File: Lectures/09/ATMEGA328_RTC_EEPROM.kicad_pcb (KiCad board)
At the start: 2 copper layers, 50.8 x 53.3 mm, 44 parts, among them J1 Serial, J2 Digital 1, J3 I2C, J4 ICSP, J5 Digital 2, Q1 IRLML6401, SW1 SW_SPST, U1 ATmega328P-AU, U2 24LC1025, U3 24LC1025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

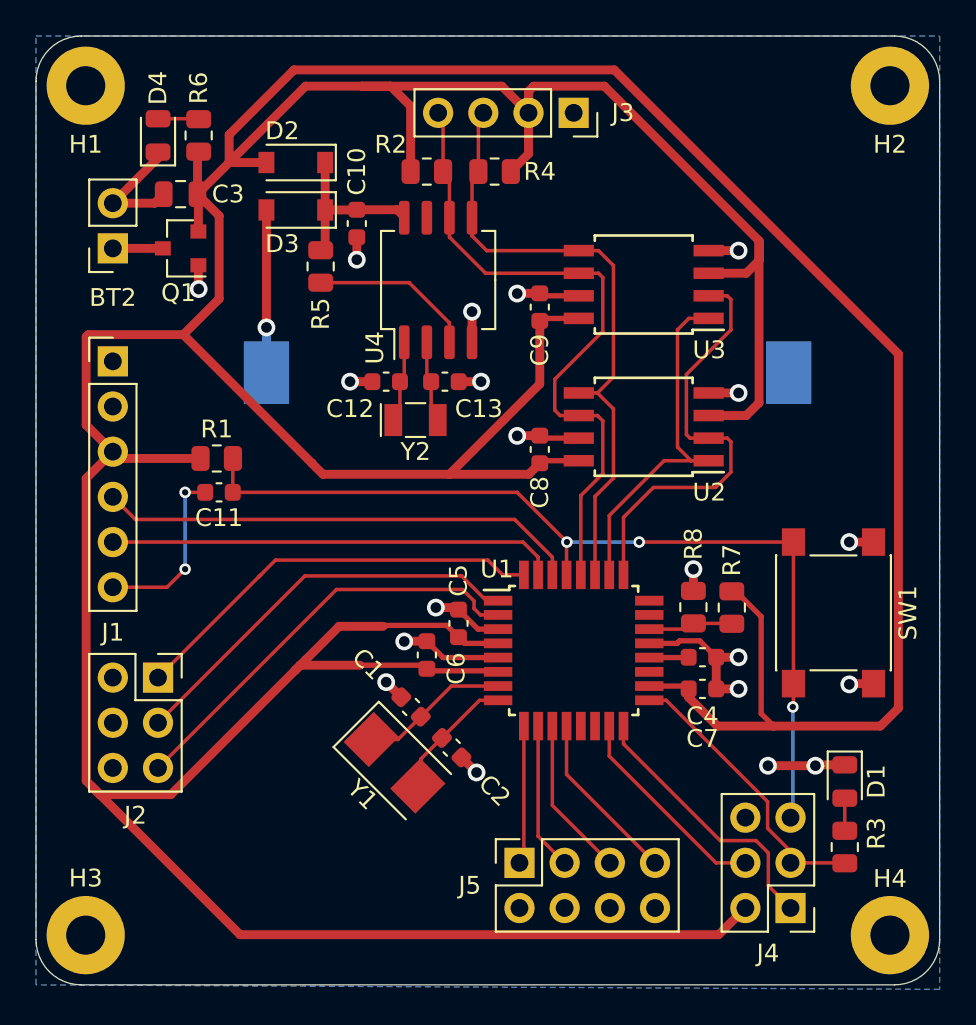
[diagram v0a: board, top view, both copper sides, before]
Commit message: Addressing and Silkscreen
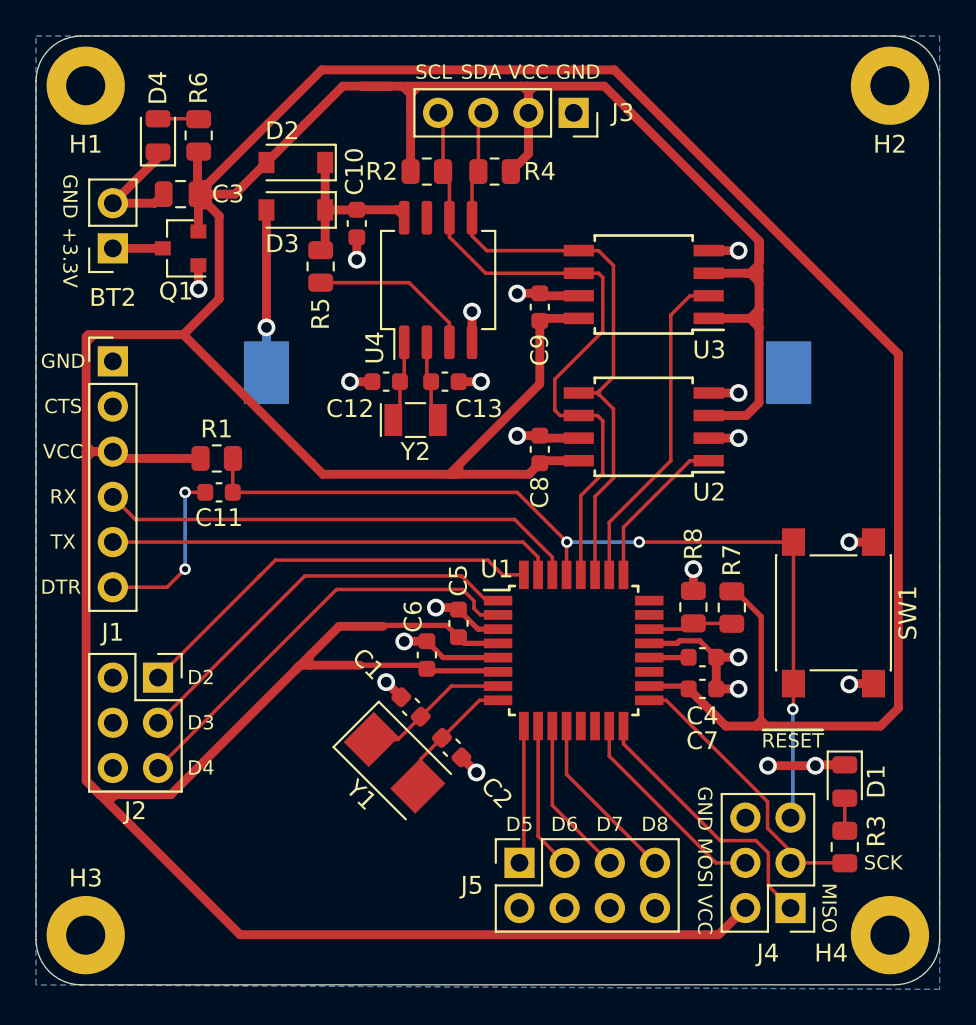
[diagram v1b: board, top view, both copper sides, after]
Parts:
- added REF**: OSHW-Logo2_7.3x6mm_SilkScreen, Symbol:OSHW-Logo2_7.3x6mm_SilkScreen, B.Cu at (141.0, 117.2)
- added e: KiCad-Logo2_5mm_SilkScreen, Symbol:KiCad-Logo2_5mm_SilkScreen, B.Cu at (141.1, 124.0)
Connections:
- U1 pad 25: /ADDR2 -> /ADDR1
- U1 pad 26: /ADDR1 -> /ADDR2
- U2 pad 2: /ADDR2 -> GND
- U3 pad 1: /ADDR1 -> /Vcc
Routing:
- net /Vcc: track 329.6 -> 345.4 mm
- net /ADDR1: track 20.5 -> 9.02 mm
- net /ADDR2: track 26.9 -> 18.6 mm
- net GND: track 53.1 -> 54.8 mm, vias 20 -> 21
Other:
- board text added: "+3.3V"
- board text added: "CTS"
- board text added: "D2"
- board text added: "D3"
- board text added: "D4"
- board text added: "D5"
- board text added: "D6"
- board text added: "D7"
- board text added: "D8"
- board text added: "DTR"
- board text added: "GND"
- board text added: "MISO"
- board text added: "MOSI"
- board text added: "RX"
- board text added: "SCK"
- board text added: "SCL"
- board text added: "SDA"
- board text added: "TX"
- board text added: "VCC"
- board text added: "~RESET"

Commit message: EEPROM addresses set by jumpers
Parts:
- removed REF**: OSHW-Logo2_7.3x6mm_SilkScreen, Symbol:OSHW-Logo2_7.3x6mm_SilkScreen
- removed e: KiCad-Logo2_5mm_SilkScreen, Symbol:KiCad-Logo2_5mm_SilkScreen
- added JP1: SJ, Jumper:SolderJumper-3_P1.3mm_Open_Pad1.0x1.5mm, F.Cu at (168.5, 101.7)
- added JP2: SJ, Jumper:SolderJumper-3_P1.3mm_Open_Pad1.0x1.5mm, F.Cu at (168.5, 97.2)
- added JP3: SJ, Jumper:SolderJumper-3_P1.3mm_Open_Pad1.0x1.5mm, F.Cu at (168.5, 93.6)
- added JP4: SJ, Jumper:SolderJumper-3_P1.3mm_Open_Pad1.0x1.5mm, F.Cu at (168.5, 89.3)
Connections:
- U1 pad 25: /ADDR1 -> Net-(U1-Pad25)
- U1 pad 26: /ADDR2 -> Net-(U1-Pad26)
- U2 pad 1: /ADDR1 -> Net-(JP1-Pad2)
- U2 pad 2: GND -> Net-(JP2-Pad2)
- U3 pad 1: /Vcc -> Net-(JP3-Pad2)
- U3 pad 2: /ADDR2 -> Net-(JP4-Pad2)
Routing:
- net GND: track 54.8 -> 74.3 mm, vias 21 -> 26
- net /ADDR2: track 18.6 -> 0.00 mm
- net /Vcc: track 345.4 -> 358.5 mm
- net /ADDR1: track 9.02 -> 0.00 mm
- net Net-(JP1-Pad2): track 0.00 -> 4.96 mm
- net Net-(JP2-Pad2): track 0.00 -> 4.96 mm
- net Net-(JP3-Pad2): track 0.00 -> 4.90 mm
- net Net-(JP4-Pad2): track 0.00 -> 4.90 mm
- added copper zone on F.Cu, net GND
